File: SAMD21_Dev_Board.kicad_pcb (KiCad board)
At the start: 2 copper layers, 55.4 x 87.4 mm, 86 parts, among them J1 SWD, J10 JST_SH_SM06B-SRSS-TB_1x06-1MP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, J11 JST_SH_SM06B-SRSS-TB_1x06-1MP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, J12 JST_SH_SM06B-SRSS-TB_1x06-1MP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, J13 JST_SH_SM06B-SRSS-TB_1x06-1MP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, J14 JST_SH_SM06B-SRSS-TB_1x06-1MP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, J15 JST_SH_SM06B-SRSS-TB_1x06-1MP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, J16 JST_SH_SM06B-SRSS-TB_1x06-1MP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, J17 Status LED, J2 USB_C_Receptacle_USB2.0_16P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

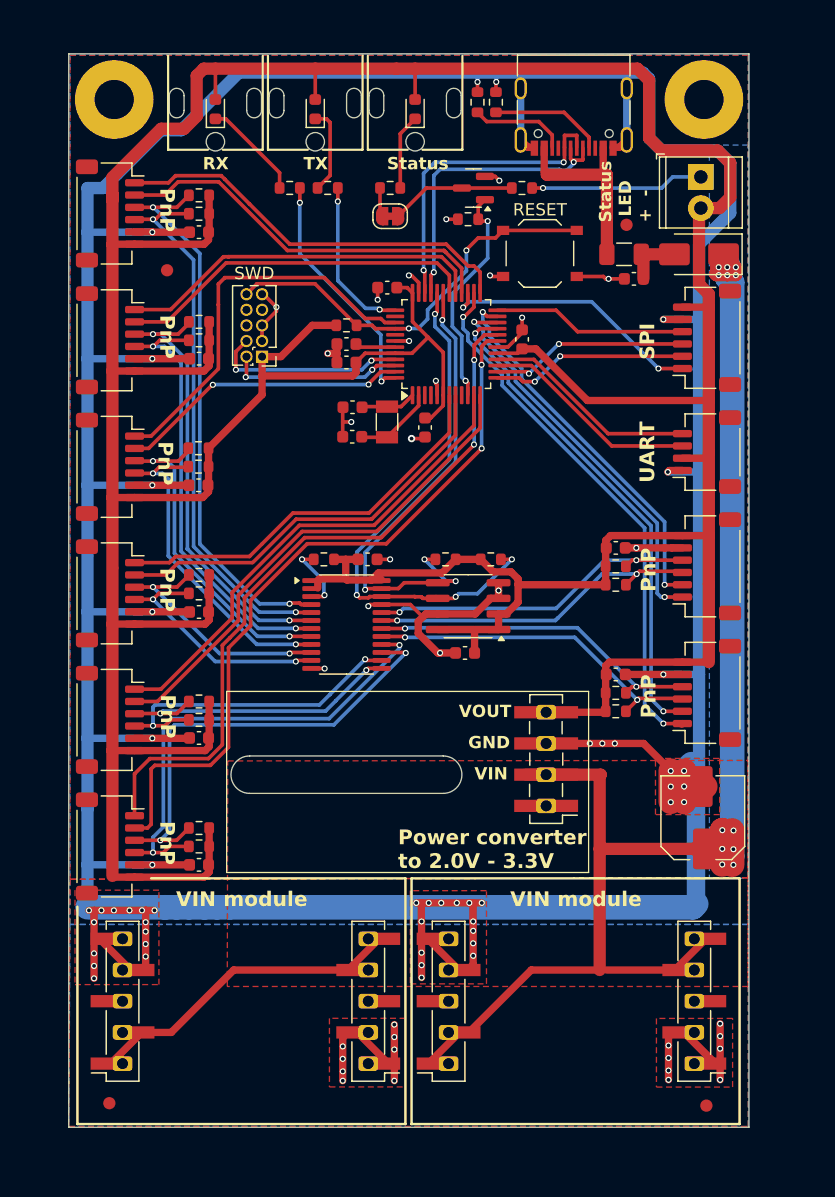
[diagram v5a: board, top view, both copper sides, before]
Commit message: Adding missing holes on the bottom side. Adding holes in the middle of the board for potential add-ons.
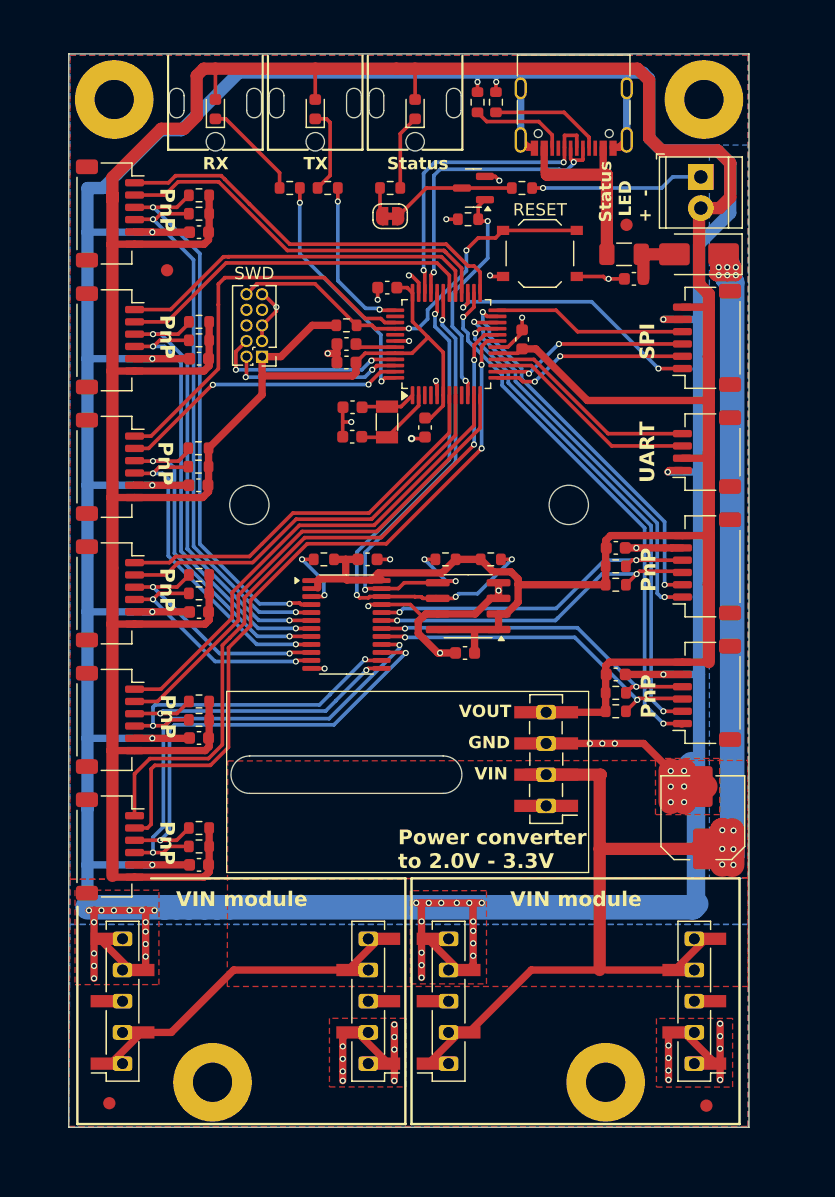
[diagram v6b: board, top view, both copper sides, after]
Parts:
- added REF**: MountingHole_3.2mm_M3_Pad, MountingHole:MountingHole_3.2mm_M3_Pad, F.Cu at (126.0, 133.5)
- added REF**: MountingHole_3.2mm_M3_Pad, MountingHole:MountingHole_3.2mm_M3_Pad, F.Cu at (94.0, 133.5)
- moved G*** 29.4 mm to (123.7, 119.6)
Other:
- outline, holes or cut-outs redrawn
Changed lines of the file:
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@@
 	(title_block
 		(title "PlugAndPlay SAMD21 Dev Board")
-		(rev "2")
+		(rev "3")
 		(company "A.B. Yazamut")
 	)
@@
 		)
 	)
+	(footprint "MountingHole:MountingHole_3.2mm_M3_Pad"
+		(locked yes)
+		(layer "F.Cu")
+		(at 94 133.5)
+		(descr "Mounting Hole 3.2mm, M3")
+		(tags "mounting hole 3.2mm m3")
+		(property "Reference" "REF**"
+			(at 0 -4.2 0)
+			(layer "F.SilkS")
+			(hide yes)
+			(effects
+				(font
+					(size 1 1)
+					(thickness 0.15)
+				)
+			)
+		)
+		(property "Value" "MountingHole_3.2mm_M3_Pad"
+			(at 0 4.2 0)
+			(layer "F.Fab")
+			(hide yes)
+			(effects
+				(font
+					(size 1 1)
+					(thickness 0.15)
+				)
+			)
+		)
+		(property "Footprint" "MountingHole:MountingHole_3.2mm_M3_Pad"
+			(at 0 0 0)
+			(unlocked yes)
+			(layer "F.Fab")
+			(hide yes)
+			(effects
+				(font
+					(size 1.27 1.27)
+					(thickness 0.15)
+				)
+			)
+		)
+		(property "Datasheet" ""
+			(at 0 0 0)
+			(unlocked yes)
+			(layer "F.Fab")
+			(hide yes)
+			(effects
+				(font
+					(size 1.27 1.27)
+					(thickness 0.15)
+				)
+			)
+		)
+		(property "Description" ""
+			(at 0 0 0)
+			(unlocked yes)
+			(layer "F.Fab")
+			(hide yes)
+			(effects
+				(font
+					(size 1.27 1.27)
+					(thickness 0.15)
+				)
+			)
+		)
+		(attr exclude_from_pos_files exclude_from_bom)
+		(fp_circle
+			(center 0 0)
+			(end 3.2 0)
+			(stroke
+				(width 0.15)
+				(type solid)
+			)
+			(fill none)
+			(layer "Cmts.User")
+		)
+		(fp_circle
+			(center 0 0)
+			(end 3.45 0)
+			(stroke
+				(width 0.05)
+				(type solid)
+			)
+			(fill none)
+			(layer "F.CrtYd")
+		)
+		(fp_text user "${REFERENCE}"
+			(at 0 0 0)
+			(layer "F.Fab")
+			(effects
+				(font
+					(size 1 1)
+					(thickness 0.15)
+				)
+			)
+		)
+		(pad "1" thru_hole circle
+			(at 0 0)
+			(size 6.4 6.4)
+			(drill 3.2)
+			(layers "*.Cu" "*.Mask")
+			(remove_unused_layers no)
+		)
+	)
 	(footprint "Resistor_SMD:R_0603_1608Metric"
 		(layer "F.Cu")
@@
 		)
 	)
+	(footprint "MountingHole:MountingHole_3.2mm_M3_Pad"
+		(locked yes)
+		(layer "F.Cu")
+		(at 126 133.5)
+		(descr "Mounting Hole 3.2mm, M3")
+		(tags "mounting hole 3.2mm m3")
+		(property "Reference" "REF**"
+			(at 0 -4.2 0)
+			(layer "F.SilkS")
+			(hide yes)
+			(effects
+				(font
+					(size 1 1)
+					(thickness 0.15)
+				)
+			)
+		)
+		(property "Value" "MountingHole_3.2mm_M3_Pad"
+			(at 0 4.2 0)
+			(layer "F.Fab")
+			(hide yes)
+			(effects
+				(font
+					(size 1 1)
+					(thickness 0.15)
+				)
+			)
+		)
+		(property "Footprint" "MountingHole:MountingHole_3.2mm_M3_Pad"
+			(at 0 0 0)
+			(unlocked yes)
+			(layer "F.Fab")
+			(hide yes)
+			(effects
+				(font
+					(size 1.27 1.27)
+					(thickness 0.15)
+				)
+			)
+		)
+		(property "Datasheet" ""
+			(at 0 0 0)
+			(unlocked yes)
+			(layer "F.Fab")
+			(hide yes)
+			(effects
+				(font
+					(size 1.27 1.27)
+					(thickness 0.15)
+				)
+			)
+		)
+		(property "Description" ""
+			(at 0 0 0)
+			(unlocked yes)
+			(layer "F.Fab")
+			(hide yes)
+			(effects
+				(font
+					(size 1.27 1.27)
+					(thickness 0.15)
+				)
+			)
+		)
+		(attr exclude_from_pos_files exclude_from_bom)
+		(fp_circle
+			(center 0 0)
+			(end 3.2 0)
+			(stroke
+				(width 0.15)
+				(type solid)
+			)
+			(fill none)
+			(layer "Cmts.User")
+		)
+		(fp_circle
+			(center 0 0)
+			(end 3.45 0)
+			(stroke
+				(width 0.05)
+				(type solid)
+			)
+			(fill none)
+			(layer "F.CrtYd")
+		)
+		(fp_text user "${REFERENCE}"
+			(at 0 0 0)
+			(layer "F.Fab")
+			(effects
+				(font
+					(size 1 1)
+					(thickness 0.15)
+				)
+			)
+		)
+		(pad "1" thru_hole circle
+			(at 0 0)
+			(size 6.4 6.4)
+			(drill 3.2)
+			(layers "*.Cu" "*.Mask")
+			(remove_unused_layers no)
+		)
+	)
 	(footprint "Button_Switch_SMD:SW_Push_1P1T_XKB_TS-1187A"
 		(layer "F.Cu")
@@
 	(footprint "Library:4P-logo-front"
 		(layer "B.Cu")
-		(at 95.021476 125.77502 -90)
+		(at 123.721476 119.57502 -90)
 		(property "Reference" "G***"
 			(at 0 0 90)
@@
 		(layer "Edge.Cuts")
 	)
+	(gr_circle
+		(center 97 86.5)
+		(end 98.6 86.5)
+		(locked yes)
+		(stroke
+			(width 0.1)
+			(type default)
+		)
+		(fill none)
+		(layer "Edge.Cuts")
+	)
 	(gr_line
 		(start 82.296 49.784)
@@
 		(layer "Edge.Cuts")
 	)
+	(gr_circle
+		(center 123 86.5)
+		(end 124.6 86.5)
+		(locked yes)
+		(stroke
+			(width 0.1)
+			(type default)
+		)
+		(fill none)
+		(layer "Edge.Cuts")
+	)
 	(gr_line
 		(start 137.668 137.16)
@@
 	)
 	(gr_text "www.4project.co.il"
-		(at 100.5 117.634286 90)
+		(at 129.2 111.434286 90)
 		(layer "B.SilkS")
 		(effects
@@
 		)
 	)
+	(group ""
+		(members "6eb83084-4077-4bcf-9b5f-4541bcea8af9" "a1cdd103-1bc1-49ba-8add-28231b7bdf4b")
+	)
 )

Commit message: Added thermal relief
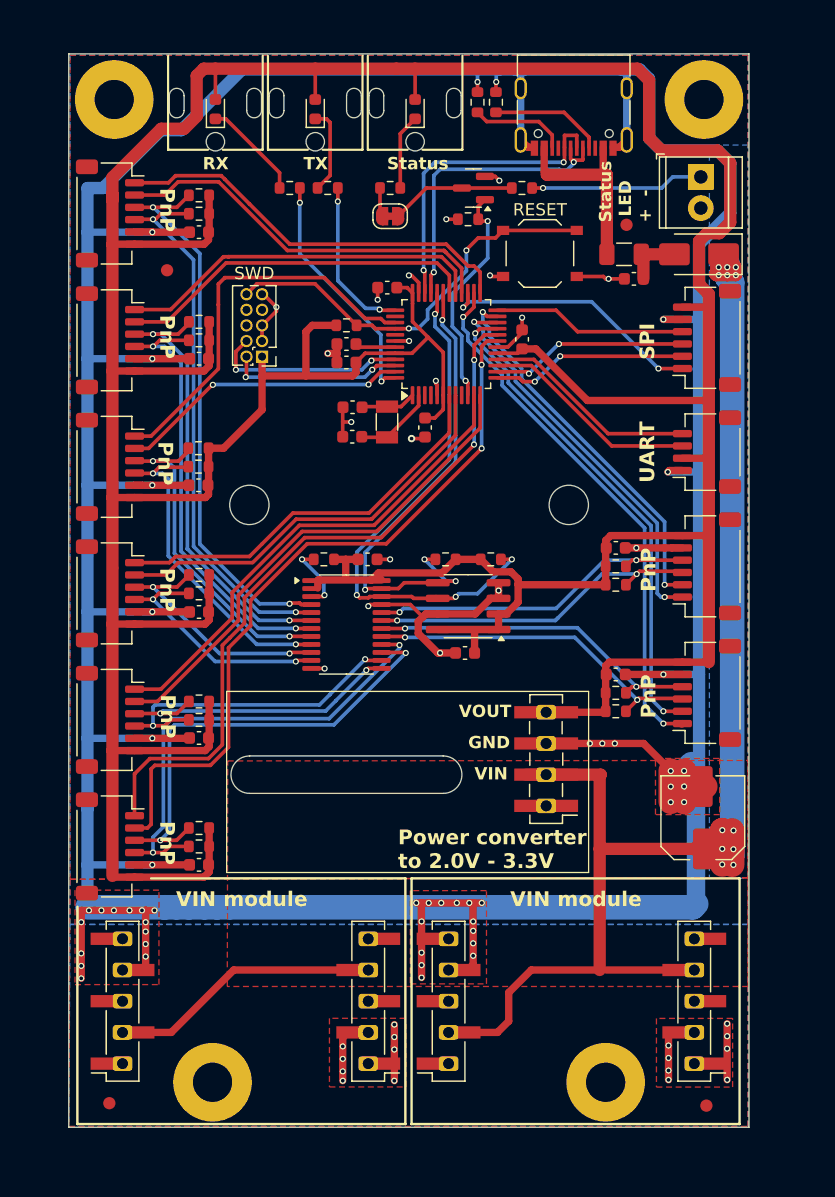
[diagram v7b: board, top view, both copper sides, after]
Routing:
- net GND: track 481.9 -> 467.9 mm
- net VDC: track 154.7 -> 142.6 mm
- net VCC: track 380.2 -> 381.0 mm

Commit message: Adding colors to GND,VCC and VDC nets. VIAs review.
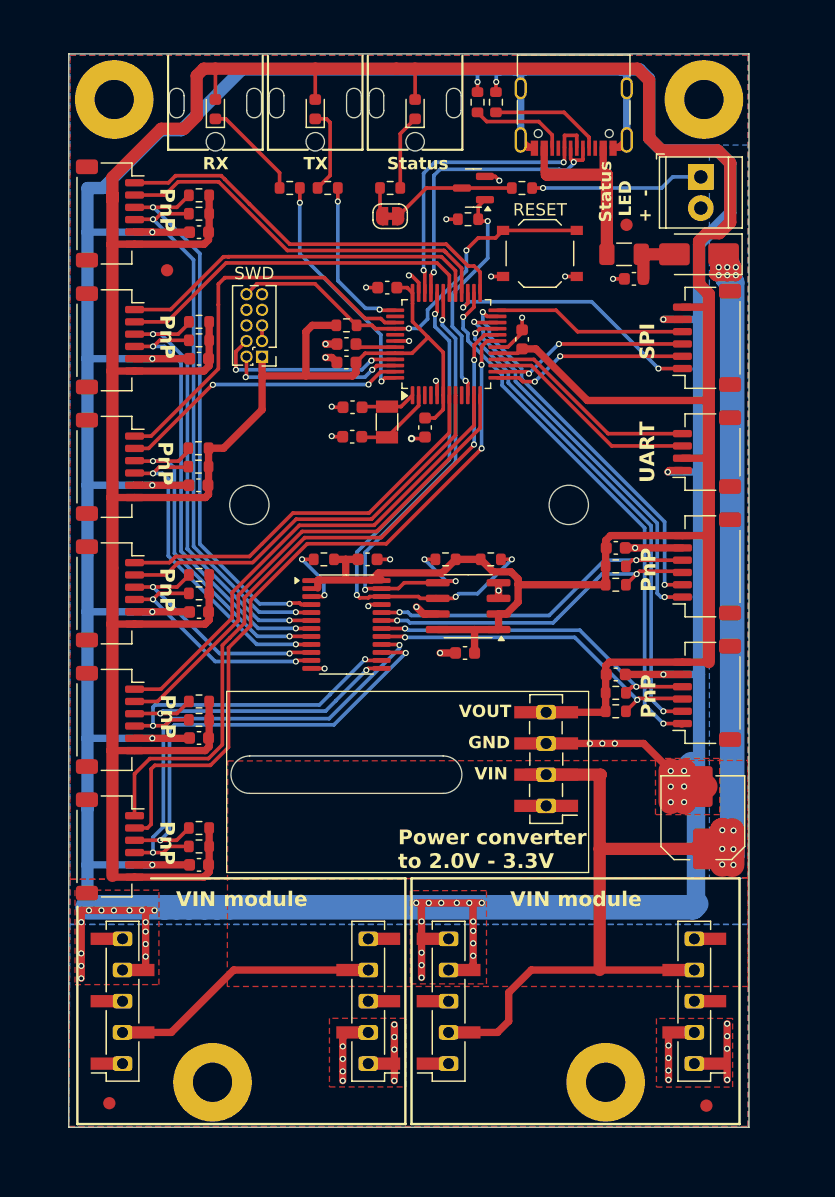
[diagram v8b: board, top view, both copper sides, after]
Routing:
- net GND: track 467.9 -> 447.4 mm, vias 83 -> 86
- net VDC: track 142.6 -> 143.2 mm
